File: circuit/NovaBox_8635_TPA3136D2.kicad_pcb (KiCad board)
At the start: 2 copper layers, 100 x 100 mm, 98 parts, among them P1 USB, P2 MH, P3 MH, P4 MH, P5 MH, Q1 IRLML6401, Q2 IRLML6401, Q3 MMBT3904, Q4 MMBT3904, Q5 IRLML6344, SW1 PIO18, SW2 PIO21, SW3 PIO8, SW4 PIO0, SW5 PIO1, SW6 ON/OFF, U1 CSR8635_MODULE, U2 CSR_DebugSmall, U3 TPA3136D2, U4 MCP6004

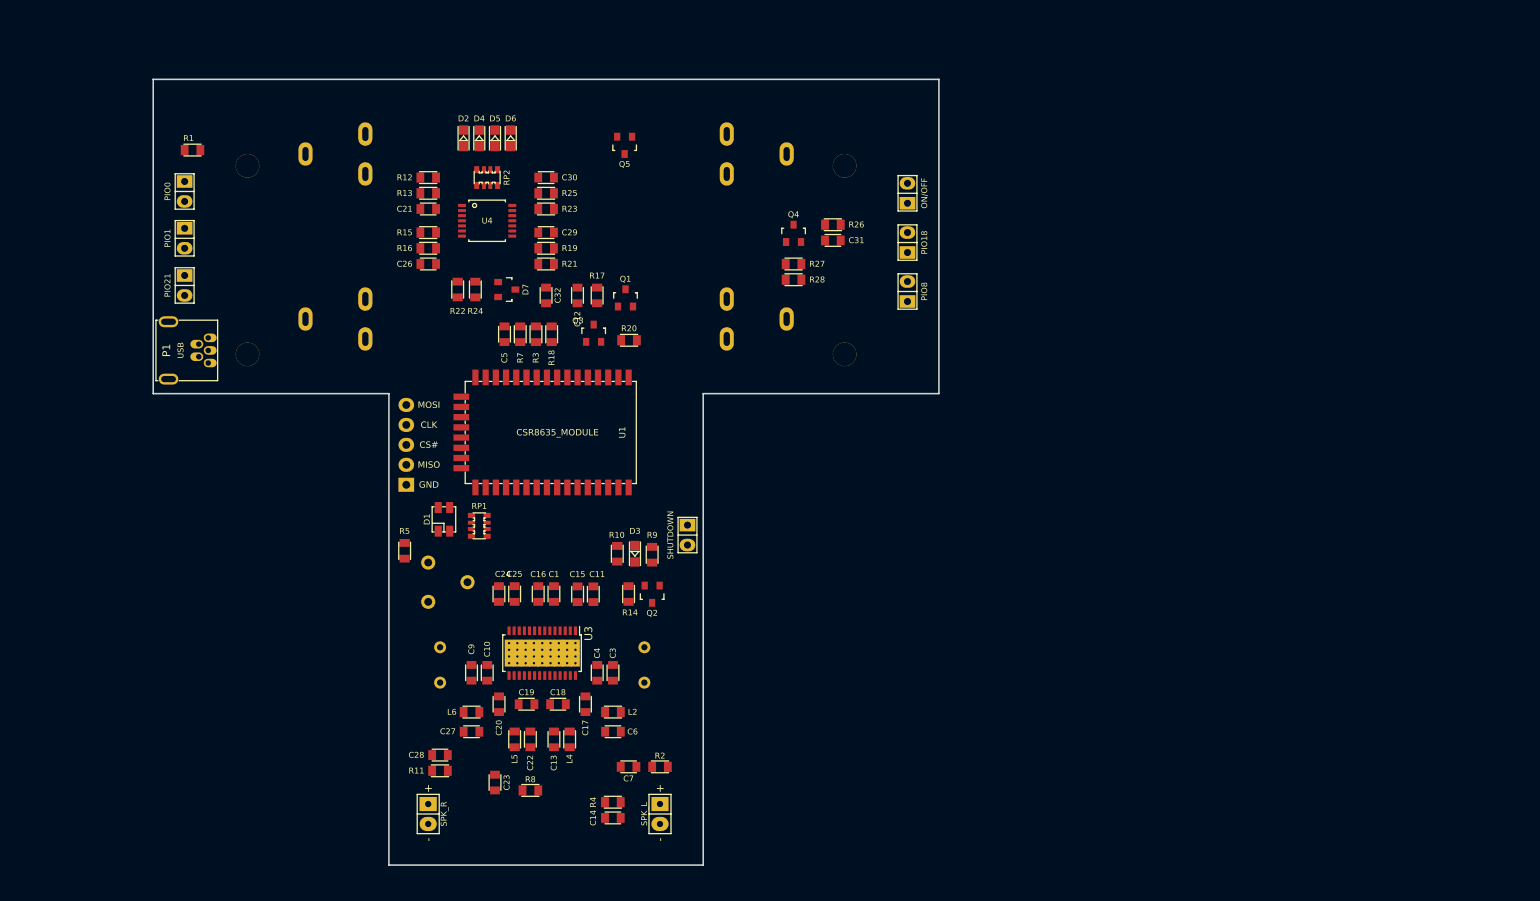
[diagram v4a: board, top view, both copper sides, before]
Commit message: 3x charger done
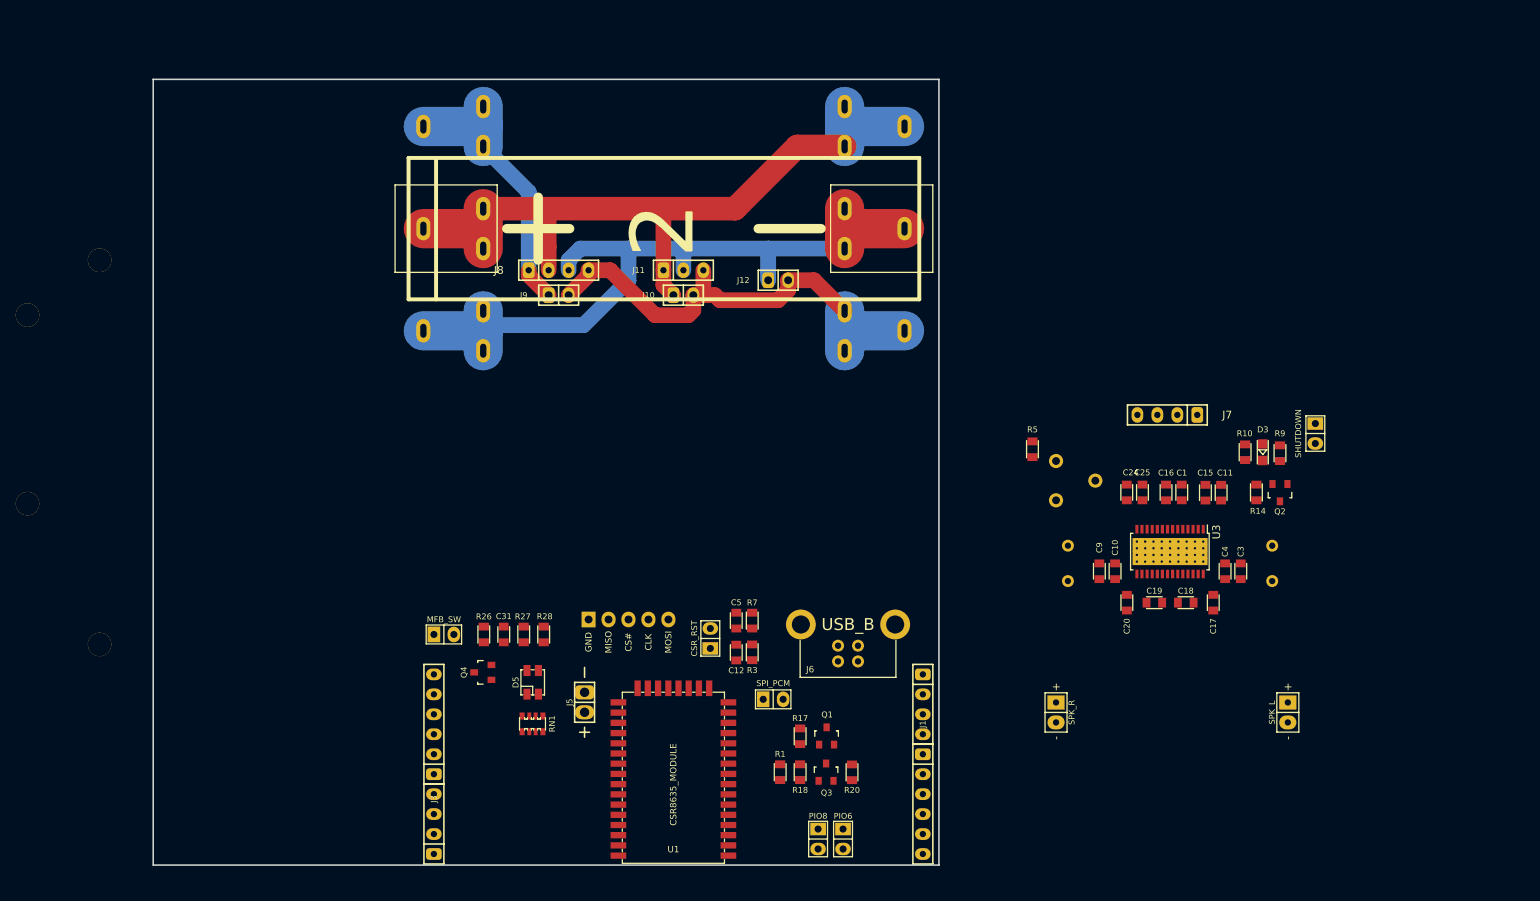
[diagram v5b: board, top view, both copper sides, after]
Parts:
- removed C13, C14, C22, C23, C27, C28, C6, C7: 1nF, NovaBox:C_0805
- removed C21, C26, C29, C30, C32: 1uF, NovaBox:C_0805
- removed D1: LED_RABG, NovaBox:PLCC4
- removed D2: BATT_E, NovaBox:LED_0805
- removed D4: BATT_L, NovaBox:LED_0805
- removed D6: BATT_H, NovaBox:LED_0805
- removed D7: Vref 2.5V, NovaBox:SOT-23
- removed L2, L4, L5, L6: 3.1A, NovaBox:R_0805
- removed P1: USB, NovaBox:USB_MiniB_THT
- removed Q5: IRLML6344, NovaBox:SOT-23
- removed R11, R2, R4, R8: 68, NovaBox:R_0805
- removed R12, R15: 180K, NovaBox:R_0805
- removed R13, R23: 390K, NovaBox:R_0805
- removed R16, R19: 360K, NovaBox:R_0805
- removed R21, R25: 680K, NovaBox:R_0805
- removed R22: 750, NovaBox:R_0805
- removed R24: 10K, NovaBox:R_0805
- removed RP1, RP2: R_Pack04, NovaBox:Resistor_Array_x4_1206
- removed SW6: ON/OFF, NovaBox:Switch_2.5mm
- removed U4: MCP6004, NovaBox:TSSOP-14_4.4x5mm_Pitch0.65mm
- added BT3: 18650, NovaBox:Batt_Holder_18650, B.Cu at (115.0, 56.0)
- added J1: CONN_01X06, NovaBox:PIN_6x1, F.Cu at (148.0, 142.2)
- added J10: CONN_01X02, NovaBox:PIN_2x1, F.Cu at (117.5, 77.5)
- added J11: CONN_01X03, NovaBox:PIN_3x1, F.Cu at (117.5, 74.3)
- added J12: CONN_01X02, NovaBox:PIN_2x1, F.Cu at (129.5, 75.6)
- added J2: CONN_01X04, NovaBox:PIN_4x1, F.Cu at (85.7, 144.8)
- added J3: CONN_01X06, NovaBox:PIN_6x1, F.Cu at (85.7, 132.1)
- added J4: CONN_01X04, NovaBox:PIN_4x1, F.Cu at (148.0, 129.5)
- added J5: CONN_01X02, NovaBox:PWR, F.Cu at (104.9, 129.3)
- added J6: USB_B, NovaBox:USB_B, F.Cu at (138.4, 119.4)
- added J7: CONN_01X04, NovaBox:PIN_4x1, F.Cu at (179.1, 92.7)
- added J8: CONN_01X04, NovaBox:PIN_4x1, F.Cu at (101.6, 74.3)
- added J9: CONN_01X02, NovaBox:PIN_2x1, F.Cu at (101.6, 77.5)
- added RN1: R_Pack04, NovaBox:Resistor_Array_x4_1206, F.Cu at (98.3, 132.0)
- BT2: moved to F.Cu
- D5: value BATT_M -> LED_RABG; footprint NovaBox:LED_0805 -> NovaBox:PLCC4
- SW1: value PIO18 -> PIO8
- SW2: value PIO21 -> PIO6
- SW3: value PIO8 -> SPI_PCM
- SW4: value PIO0 -> CSR_RST
- SW5: value PIO1 -> MFB_SW
- moved SW2 109.5 mm to (137.8, 146.7)
- moved R1 108.9 mm to (129.8, 138.2), turned to 90 degrees
- moved P2 105.7 mm to (34.0, 80.0)
- moved P4 105.7 mm to (34.0, 104.0)
- moved SW4 87.8 mm to (120.9, 121.2), turned to 270 degrees
- moved SPK1 80.9 mm to (194.4, 130.6)
- moved SPK2 80.9 mm to (164.9, 130.6)
- moved C1 80.9 mm to (180.9, 102.6)
- moved C16 80.9 mm to (178.9, 102.6)
- moved C24 80.9 mm to (173.9, 102.6)
- moved C25 80.9 mm to (175.9, 102.6)
- moved D3 80.9 mm to (191.2, 97.5)
- moved Q2 80.9 mm to (193.4, 102.6)
- moved R10 80.9 mm to (189.0, 97.5)
- moved R14 80.9 mm to (190.4, 102.6)
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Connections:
- BT1 pad 1: +4V -> /BAT1+
- BT1 pad 2: /-BATT -> /BAT-
- BT2 pad 1: +8V -> /BAT2+
- BT2 pad 2: +4V -> /BAT1+
- C11 pad 1: Net-(C11-Pad1) -> /IN_LP
- C15 pad 1: Net-(C15-Pad1) -> /IN_LN
- C24 pad 1: Net-(C24-Pad1) -> /IN_RP
- C25 pad 1: Net-(C25-Pad1) -> /IN_RN
- C5 pad 1: CSR_RST -> Net-(C5-Pad1)
- D5 pad 1: GND -> Net-(D5-Pad1)
- D5 pad 2: Net-(D5-Pad2) -> +4V
- Q4 pad 3: PWER_E -> Net-(Q4-Pad3)
- R1 pad 1: 1V8 -> Net-(R1-Pad1)
- R1 pad 2: Net-(R1-Pad2) -> +1V8
- R18 pad 2: 1V8 -> +1V8
- R26 pad 1: PWER_E -> Net-(Q4-Pad3)
- R3 pad 1: 1V8 -> +1V8
- R3 pad 2: SPI_PCM -> Net-(R3-Pad2)
- R7 pad 1: 1V8 -> +1V8
- R7 pad 2: CSR_RST -> Net-(C5-Pad1)
- SPK1 pad 1: Net-(C6-Pad2) -> Net-(C17-Pad1)
- SPK1 pad 2: Net-(C13-Pad2) -> Net-(C18-Pad1)
- SPK2 pad 1: Net-(C27-Pad2) -> Net-(C20-Pad1)
- SPK2 pad 2: Net-(C22-Pad2) -> Net-(C19-Pad1)
- SW1 pad 1: PIO18 -> Net-(R1-Pad1)
- SW1 pad 2: Net-(R1-Pad2) -> PIO8
- SW2 pad 1: PIO21 -> Net-(R1-Pad1)
- SW2 pad 2: Net-(R1-Pad2) -> PIO6
- SW3 pad 1: PIO8 -> SPI_PCM
- SW3 pad 2: Net-(R1-Pad2) -> Net-(R3-Pad2)
- SW4 pad 1: PIO0 -> CSR_RST
- SW4 pad 2: Net-(R1-Pad2) -> Net-(C5-Pad1)
- SW5 pad 1: PIO1 -> MFB
- SW5 pad 2: Net-(R1-Pad2) -> Net-(Q4-Pad3)
- U1 pad 1: (no net) -> PIO6
- U1 pad 10: 1V8 -> +1V8
- U1 pad 11: (no net) -> /PI016
- U1 pad 14: PIO21 -> /PIO21
- U1 pad 15: PIO18 -> /PIO18
- U1 pad 28: LED0 -> LED_R
- U1 pad 29: LED2 -> LED_B
- U1 pad 3: PIO1 -> /PIO1
- U1 pad 30: PWER_E -> MFB
- U1 pad 31: (no net) -> /MIC_BIAS
- U1 pad 32: (no net) -> /LINE_BP
- U1 pad 33: (no net) -> /LINE_BN
- U1 pad 34: (no net) -> /MIC_AP
- U1 pad 35: (no net) -> /MIC_AN
- U1 pad 36: Net-(C25-Pad1) -> /SPK_RN
- U1 pad 37: Net-(C24-Pad1) -> /SPK_RP
- U1 pad 38: Net-(C15-Pad1) -> /SPK_LN
- U1 pad 39: Net-(C11-Pad1) -> /SPK_LP
- U1 pad 4: PIO0 -> /PIO0
- U1 pad 5: LED1 -> LED_G
- U1 pad 7: (no net) -> /PIO17
- U1 pad 8: (no net) -> /PIO9
- U1 pad 9: (no net) -> /PIO7
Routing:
- net /BAT1+: track 0.00 -> 95.0 mm
- net /BAT2+: track 0.00 -> 94.2 mm
- net /BAT-: track 0.00 -> 60.9 mm
- net /BAT3+: track 0.00 -> 35.1 mm
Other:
- outline, holes or cut-outs redrawn
- board text added: "1"
- board text added: "2"
- board text added: "3"

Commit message: charger done; CSR breakout layout done
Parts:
- removed D5: LED_RABG, NovaBox:PLCC4
- removed RN1: R_Pack04, NovaBox:Resistor_Array_x4_1206
- added D1: LED_R, NovaBox:LED-3MM, F.Cu at (107.5, 110.5)
- added D2: LED_G, NovaBox:LED-3MM, F.Cu at (98.5, 110.5)
- added D4: LED_B, NovaBox:LED-3MM, F.Cu at (103.0, 110.5)
- added J13: CONN_01X02, NovaBox:PWR, F.Cu at (62.5, 111.0)
- added J14: CONN_01X04, NovaBox:PIN_4x1, F.Cu at (64.1, 52.8)
- added R2: 1K, NovaBox:R_10MM, F.Cu at (105.5, 120.6)
- added R4: 1K, NovaBox:R_10MM, F.Cu at (100.5, 120.5)
- added R8: 1K, NovaBox:R_10MM, F.Cu at (103.0, 120.5)
- BT1, BT2, BT3: footprint NovaBox:Batt_Holder_18650 -> NovaBox:Batt_Holder_18650_mini
- C1, C11, C12, C15, C16, C24, C25, C31: footprint NovaBox:C_0805 -> NovaBox:C_1206
- C10, C3, C4, C5, C9: footprint NovaBox:C_0805 -> NovaBox:C_5MM
- D3: footprint NovaBox:LED_0805 -> NovaBox:LED-3MM
- J10, J12, J9: footprint NovaBox:PIN_2x1 -> NovaBox:PWR
- J6: value USB_B -> USB
- R1, R17, R18, R20, R26, R27, R28, R3, R7: footprint NovaBox:R_0805 -> NovaBox:R_10MM
- moved SPK1 142.4 mm to (52.0, 128.5), turned to 270 degrees
- moved C2 133.8 mm to (62.5, 143.5), turned to 0 degrees
- moved C3 128.6 mm to (61.4, 132.9), turned to 180 degrees
- moved C17 128.2 mm to (57.4, 129.4), turned to 0 degrees
- moved S1 128.0 mm to (78.9, 142.4), turned to 0 degrees
- moved Q2 127.0 mm to (71.4, 137.9), turned to 90 degrees
- moved C4 126.4 mm to (61.4, 130.9), turned to 180 degrees
- moved C18 124.4 mm to (57.4, 125.9), turned to 90 degrees
- moved R9 123.7 mm to (76.4, 137.9), turned to 0 degrees
- moved R14 123.3 mm to (71.4, 134.9), turned to 180 degrees
- moved D3 120.9 mm to (76.5, 135.7), turned to 0 degrees
- moved C19 120.1 mm to (57.4, 121.9), turned to 270 degrees
- moved R10 118.0 mm to (76.5, 133.5), turned to 180 degrees
- moved C11 117.9 mm to (71.4, 130.4), turned to 180 degrees
- moved C20 116.5 mm to (57.4, 118.4), turned to 0 degrees
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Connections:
- Q1 pad 3: +4V -> /4V
- R17 pad 1: +4V -> /4V
- R18 pad 2: +1V8 -> /1.8V
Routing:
- net /BAT1+: track 95.0 -> 93.9 mm
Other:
- outline, holes or cut-outs redrawn
- board text added: "+1.8V"
- board text added: "+4V"
- board text added: "EN_DEV"
- board text added: "GND"
- board text added: "LINE_BN"
- board text added: "LINE_BP"
- board text added: "MFB"
- board text added: "MIC_AN"
- board text added: "MIC_AP"
- board text added: "MIC_BIAS"
- board text added: "PIO0"
- board text added: "PIO1"
- board text added: "PIO16"
- board text added: "PIO17"
- board text added: "PIO6"
- board text added: "PIO7"
- board text added: "PIO8"
- board text added: "PIO9"
- board text added: "SPK_LN"
- board text added: "SPK_RN"
- board text added: "SPK_RP"
- board text added: "SPL_LP"

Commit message: first draft! hip hip hurray!!!
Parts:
- removed J3: CONN_01X06, NovaBox:PIN_6x1
- removed J4: CONN_01X04, NovaBox:PIN_4x1
- C2, C8, R6, U2: moved to F.Cu
- D3: value LED -> FAULT
- J1: value CONN_01X06 -> CONN_01X13; footprint NovaBox:PIN_6x1 -> NovaBox:PIN_13x1
- J2: value CONN_01X04 -> CONN_01X10; footprint NovaBox:PIN_4x1 -> NovaBox:PIN_10x1
- J6: value USB -> USB_B
- R10, R14, R5, R9: footprint NovaBox:R_0805 -> NovaBox:R_10MM
- moved J14 29.3 mm to (76.6, 79.3), turned to 270 degrees
- moved R20 18.2 mm to (63.1, 83.7), turned to 180 degrees
- moved BT1 18.0 mm to (115.0, 100.0)
- moved BT2 18.0 mm to (115.0, 87.0)
- moved BT3 18.0 mm to (115.0, 74.0)
- moved J10 18.0 mm to (117.5, 95.5)
- moved J11 18.0 mm to (117.5, 92.3)
- moved J12 18.0 mm to (129.5, 93.6)
- moved J8 18.0 mm to (101.6, 92.3)
- moved J9 18.0 mm to (101.6, 95.5)
- moved P2 18.0 mm to (102.0, 72.0)
- moved P3 18.0 mm to (132.0, 102.0)
- moved P4 18.0 mm to (102.0, 102.0)
- moved P5 18.0 mm to (132.0, 72.0)
- moved R18 15.2 mm to (63.1, 81.2), turned to 0 degrees
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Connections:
- J1 pad 1: /PIO9 -> PIO6
- J1 pad 2: /PIO17 -> PIO8
- J1 pad 3: /PIO0 -> /PIO1
- J1 pad 4: /PIO1 -> /PIO0
- J1 pad 5: PIO8 -> /AIO0
- J1 pad 6: PIO6 -> /PIO17
- U1 pad 12: (no net) -> /JACK_DET
- U1 pad 13: (no net) -> /LINE_MIC_PIO
- U1 pad 6: (no net) -> /AIO0
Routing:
- net +8V: track 0.00 -> 133.0 mm, vias 0 -> 1
- net +4V: track 0.00 -> 71.9 mm
- net GND: track 0.00 -> 48.9 mm
- net Net-(R9-Pad1): track 0.00 -> 42.5 mm
- net MFB: track 0.00 -> 31.9 mm
- net LED_G: track 0.00 -> 30.2 mm, vias 0 -> 1
- net /PIO18: track 0.00 -> 30.2 mm
- net Net-(C16-Pad2): track 0.00 -> 29.7 mm, vias 0 -> 1
- net /PIO21: track 0.00 -> 29.7 mm
- net /LINE_MIC_PIO: track 0.00 -> 29.2 mm
- net /JACK_DET: track 0.00 -> 28.6 mm
- net Net-(Q2-Pad1): track 0.00 -> 28.2 mm
- net /PIO7: track 0.00 -> 28.2 mm
- net /PI016: track 0.00 -> 28.1 mm
- net /PIO9: track 0.00 -> 27.6 mm
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- added copper zone on B.Cu, net GND
- added copper zone on F.Cu, net GND
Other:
- board size 100 x 100 mm -> 100 x 82 mm
- board text added: "AIO0"
- board text added: "IN_LN"
- board text added: "IN_LP"
- board text added: "IN_RN"
- board text added: "IN_RP"
- board text added: "JACK_DET"
- board text added: "LINE MIC_PIO"
- board text added: "PIO18"
- board text added: "PIO21"

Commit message: almost done
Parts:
- removed P2, P3, P4, P5: MH, NovaBox:MountingHole
- added J3: CONN_01X02, NovaBox:PIN_2x1, F.Cu at (96.0, 132.3)
- added REF**: HOLE_1MM, NovaBox:HOLE_1MM, F.Cu at (146.0, 106.5)
- added REF**: HOLE_1MM, NovaBox:HOLE_1MM, F.Cu at (118.0, 106.5)
- added REF**: HOLE_1MM, NovaBox:HOLE_1MM, F.Cu at (83.5, 146.5)
- added REF**: HOLE_1MM, NovaBox:HOLE_1MM, F.Cu at (83.5, 111.5)
- added REF**: HOLE_1MM, NovaBox:HOLE_1MM, F.Cu at (95.0, 106.5)
- added REF**: HOLE_1MM, NovaBox:HOLE_1MM, F.Cu at (79.5, 103.0)
- added REF**: HOLE_1MM, NovaBox:HOLE_1MM, F.Cu at (60.0, 88.5)
- added REF**: HOLE_1MM, NovaBox:HOLE_1MM, F.Cu at (73.5, 88.5)
- added REF**: HOLE_1MM, NovaBox:HOLE_1MM, F.Cu at (79.5, 74.0)
- J1: value CONN_01X13 -> CONN_01X11; footprint NovaBox:PIN_13x1 -> NovaBox:PIN_11x1
- J2: value CONN_01X10 -> CONN_01X15; footprint NovaBox:PIN_10x1 -> NovaBox:PIN_15x1
- U2: moved to B.Cu
- moved J2 62.6 mm to (148.0, 130.2)
- moved J1 62.3 mm to (85.7, 135.3)
- moved U2 4.67 mm to (115.4, 117.0), turned to 270 degrees
- moved SW5 2.84 mm to (93.3, 123.8), turned to 270 degrees
- moved SPK1 0.70 mm to (52.7, 124.7)
- moved SPK2 0.70 mm to (52.7, 115.7)
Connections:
- J1 pad 1: PIO6 -> /SPK_LP
- J1 pad 10: /JACK_DET -> MFB
- J1 pad 11: /LINE_MIC_PIO -> GND
- J1 pad 2: PIO8 -> /SPK_LN
- J1 pad 3: /PIO1 -> /SPK_RP
- J1 pad 4: /PIO0 -> /SPK_RN
- J1 pad 5: /AIO0 -> /MIC_AN
- J1 pad 6: /PIO17 -> /MIC_AP
- J1 pad 7: /PIO9 -> /LINE_BN
- J1 pad 8: /PIO7 -> /LINE_BP
- J1 pad 9: /PI016 -> /MIC_BIAS
- J2 pad 1: /SPK_LP -> PIO6
- J2 pad 10: MFB -> /PI016
- J2 pad 2: /SPK_LN -> PIO8
- J2 pad 3: /SPK_RP -> /PIO1
- J2 pad 4: /SPK_RN -> /PIO0
- J2 pad 5: /MIC_AN -> /AIO0
- J2 pad 6: /MIC_AP -> /PIO17
- J2 pad 7: /LINE_BN -> /PIO9
- J2 pad 8: /LINE_BP -> /PIO7
- J2 pad 9: /MIC_BIAS -> +1V8
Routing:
- net +1V8: track 18.2 -> 28.7 mm
- net Net-(U1-Pad24): track 6.43 -> 14.7 mm
- net Net-(U1-Pad23): track 6.51 -> 11.6 mm
- net MFB: track 31.9 -> 36.4 mm
- net +4V: track 71.9 -> 75.9 mm
- net Net-(U1-Pad21): track 7.54 -> 5.50 mm
- net Net-(U1-Pad22): track 7.02 -> 8.72 mm
- net /LINE_MIC_PIO: track 29.2 -> 30.2 mm
- net /PI016: track 28.1 -> 29.2 mm
- net /PIO21: track 29.7 -> 30.7 mm
- net /PIO18: track 30.2 -> 31.2 mm
- net /JACK_DET: track 28.6 -> 29.7 mm
- net Net-(C18-Pad1): track 10.0 -> 9.31 mm
- net Net-(C20-Pad1): track 11.2 -> 10.5 mm
- net Net-(C19-Pad1): track 9.95 -> 9.24 mm
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- added copper zone on B.Cu, net (none)
- added copper zone on F.Cu, net (none)
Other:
- outline, holes or cut-outs redrawn
- board text added: "2018 oct 14"
- board text added: "POWER"
